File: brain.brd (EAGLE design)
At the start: 100 x 80 mm, 20 parts, among them U1 TINY45-20-DIP, U4 TINY45-20-DIP

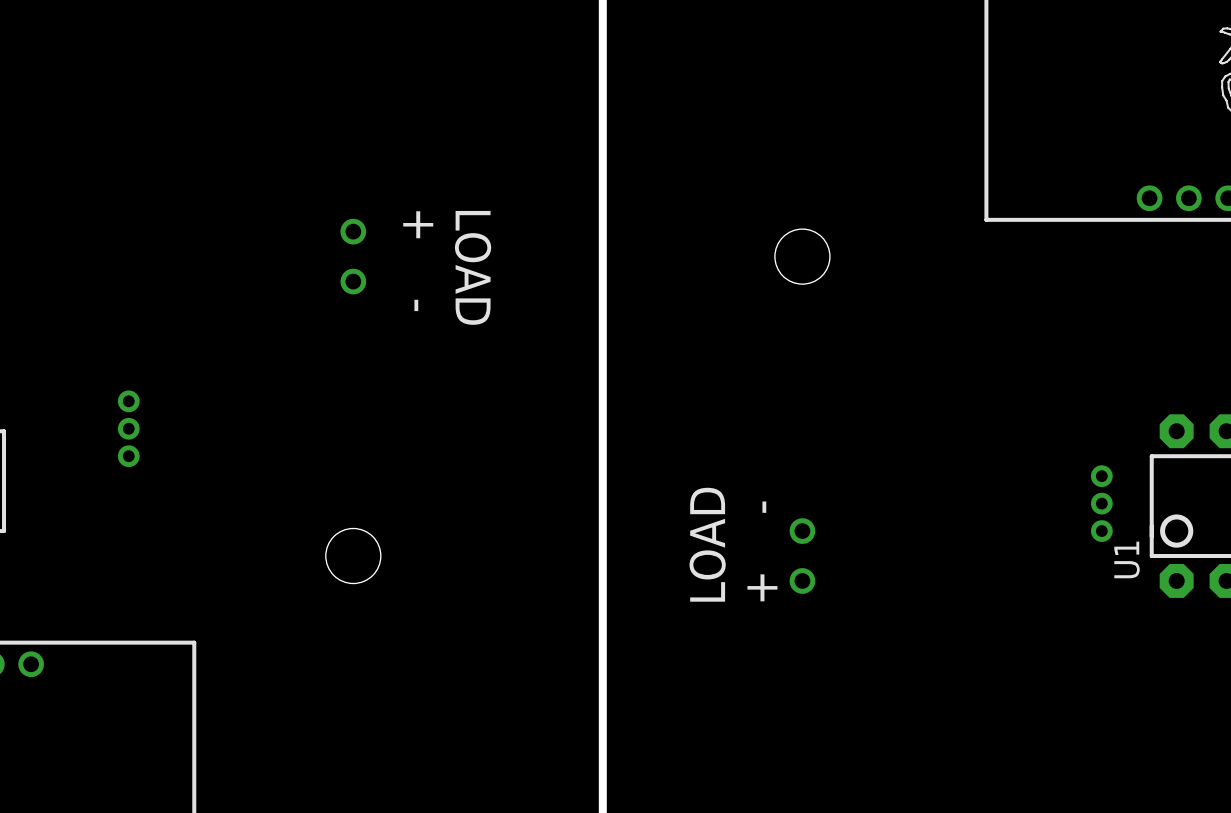
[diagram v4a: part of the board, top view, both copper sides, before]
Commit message: Switched the LDO to the ST device.
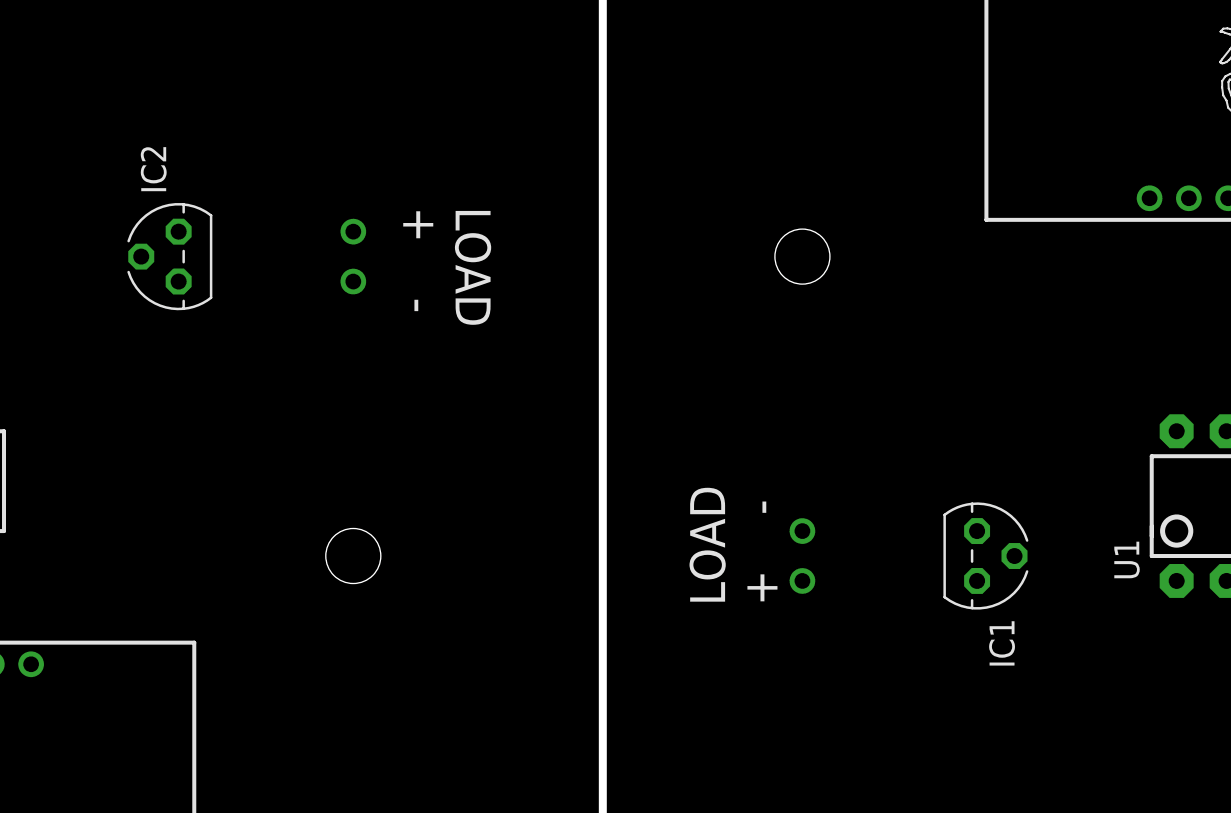
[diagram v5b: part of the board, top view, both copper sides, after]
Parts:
- removed U$2, U$5: LP2950, seniordesign:LP2950
- added IC1, IC2: LP2950ACZ-3.3, v-reg:TO92
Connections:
- net GND1: now also IC1.2; no longer U$2.GND
- net GND2: now also IC2.2; no longer U$5.GND
- net VCC1: now also IC1.1; no longer U$2.VOUT
- net VIN1: now also IC1.3; no longer U$2.VIN
- net VIN2: now also IC2.3; no longer U$5.VIN
- net VOUT2: now also IC2.1; no longer U$5.VOUT
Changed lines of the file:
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@@
 <setting verticaltext="up"/>
 </settings>
-<grid distance="0.05" unitdist="inch" unit="inch" style="dots" multiple="1" display="yes" altdistance="0.025" altunitdist="inch" altunit="inch"/>
+<grid distance="0.05" unitdist="inch" unit="inch" style="dots" multiple="1" display="no" altdistance="0.025" altunitdist="inch" altunit="inch"/>
 <layers>
 <layer number="1" name="Top" color="4" fill="1" visible="yes" active="yes"/>
@@
 <layer number="27" name="tValues" color="7" fill="1" visible="yes" active="yes"/>
 <layer number="28" name="bValues" color="7" fill="1" visible="yes" active="yes"/>
-<layer number="29" name="tStop" color="7" fill="3" visible="no" active="yes"/>
-<layer number="30" name="bStop" color="7" fill="6" visible="no" active="yes"/>
-<layer number="31" name="tCream" color="7" fill="4" visible="no" active="yes"/>
-<layer number="32" name="bCream" color="7" fill="5" visible="no" active="yes"/>
-<layer number="33" name="tFinish" color="6" fill="3" visible="no" active="yes"/>
-<layer number="34" name="bFinish" color="6" fill="6" visible="no" active="yes"/>
-<layer number="35" name="tGlue" color="7" fill="4" visible="no" active="yes"/>
-<layer number="36" name="bGlue" color="7" fill="5" visible="no" active="yes"/>
-<layer number="37" name="tTest" color="7" fill="1" visible="no" active="yes"/>
-<layer number="38" name="bTest" color="7" fill="1" visible="no" active="yes"/>
+<layer number="29" name="tStop" color="7" fill="3" visible="yes" active="yes"/>
+<layer number="30" name="bStop" color="7" fill="6" visible="yes" active="yes"/>
+<layer number="31" name="tCream" color="7" fill="4" visible="yes" active="yes"/>
+<layer number="32" name="bCream" color="7" fill="5" visible="yes" active="yes"/>
+<layer number="33" name="tFinish" color="6" fill="3" visible="yes" active="yes"/>
+<layer number="34" name="bFinish" color="6" fill="6" visible="yes" active="yes"/>
+<layer number="35" name="tGlue" color="7" fill="4" visible="yes" active="yes"/>
+<layer number="36" name="bGlue" color="7" fill="5" visible="yes" active="yes"/>
+<layer number="37" name="tTest" color="7" fill="1" visible="yes" active="yes"/>
+<layer number="38" name="bTest" color="7" fill="1" visible="yes" active="yes"/>
 <layer number="39" name="tKeepout" color="4" fill="11" visible="yes" active="yes"/>
 <layer number="40" name="bKeepout" color="1" fill="11" visible="yes" active="yes"/>
@@
 <layer number="42" name="bRestrict" color="1" fill="10" visible="yes" active="yes"/>
 <layer number="43" name="vRestrict" color="2" fill="10" visible="yes" active="yes"/>
-<layer number="44" name="Drills" color="7" fill="1" visible="no" active="yes"/>
+<layer number="44" name="Drills" color="7" fill="1" visible="yes" active="yes"/>
 <layer number="45" name="Holes" color="7" fill="1" visible="yes" active="yes"/>
-<layer number="46" name="Milling" color="3" fill="1" visible="no" active="yes"/>
-<layer number="47" name="Measures" color="7" fill="1" visible="no" active="yes"/>
+<layer number="46" name="Milling" color="3" fill="1" visible="yes" active="yes"/>
+<layer number="47" name="Measures" color="7" fill="1" visible="yes" active="yes"/>
 <layer number="48" name="Document" color="7" fill="1" visible="yes" active="yes"/>
 <layer number="49" name="Reference" color="7" fill="1" visible="yes" active="yes"/>
@@
 <layer number="100" name="Muster" color="7" fill="1" visible="no" active="no"/>
 <layer number="101" name="Patch_Top" color="12" fill="4" visible="yes" active="yes"/>
-<layer number="102" name="Vscore" color="7" fill="1" visible="yes" active="yes"/>
+<layer number="102" name="Vscore" color="12" fill="1" visible="yes" active="yes"/>
 <layer number="103" name="tMap" color="7" fill="1" visible="yes" active="yes"/>
 <layer number="104" name="Name" color="16" fill="1" visible="yes" active="yes"/>
@@
 <text x="40.64" y="52.07" size="1.778" layer="21" rot="SR270">LOAD
 +    -</text>
+<wire x1="50.8" y1="0" x2="50.8" y2="80.01" width="0.4064" layer="102"/>
 </plain>
 <attributes>
@@
 <element name="U2" library="SparkFun-Connectors" package="AUDIO-JACK" value="" x="95.25" y="22.86" rot="R180"/>
 <element name="U3" library="SparkFun-Connectors" package="AUDIO-JACK" value="" x="95.25" y="8.89" rot="R180"/>
-<element name="U$2" library="seniordesign" package="LP2950" value="LP2950" x="76.2" y="35.56" rot="R90"/>
 <element name="U$3" library="seniordesign" package="SUNNYBUDDYMOUNT" value="SUNNYBUDDYMOUNT" x="59.69" y="49.53"/>
 <element name="XB2" library="maxstream" package="XBEE-PRO" value="XBEE-PRO" x="12.7" y="17.78" rot="R90">
@@
 <attribute name="OC_FARNELL" value="176432" x="-21.59" y="-36.83" size="1.778" layer="27" rot="R90" display="off"/>
 </element>
-<element name="U$5" library="seniordesign" package="LP2950" value="LP2950" x="26.67" y="39.37" rot="R90"/>
 <element name="U$6" library="seniordesign" package="SUNNYBUDDYMOUNT" value="SUNNYBUDDYMOUNT" x="39.37" y="34.29" rot="R180"/>
 <element name="C1" library="rcl" package="C050-025X075" value="bypass" x="12.7" y="2.54"/>
@@
 <attribute name="MF" value="" x="17.78" y="73.66" size="1.778" layer="27" rot="R180" display="off"/>
 </element>
+<element name="IC1" library="v-reg" package="TO92" value="LP2950ACZ-3.3" x="69.85" y="34.29" rot="R270"/>
+<element name="IC2" library="v-reg" package="TO92" value="LP2950ACZ-3.3" x="29.21" y="49.53" rot="R90"/>
 </elements>
 <signals>
@@
 </signal>
 <signal name="VIN2">
-<contactref element="U$5" pad="VIN"/>
 <contactref element="U$6" pad="P$1"/>
-<wire x1="26.67" y1="39.37" x2="38.1" y2="50.8" width="0" layer="19" extent="1-1"/>
+<contactref element="IC2" pad="3"/>
+<wire x1="29.21" y1="50.8" x2="38.1" y2="50.8" width="0" layer="19" extent="1-1"/>
 </signal>
 <signal name="N$8">
@@
 <signal name="VOUT2">
 <contactref element="XB2" pad="1"/>
-<contactref element="U$5" pad="VOUT"/>
 <contactref element="C1" pad="1"/>
 <contactref element="U4" pad="8"/>
 <contactref element="C2" pad="1"/>
-<wire x1="11.43" y1="41.91" x2="26.67" y2="42.164" width="0" layer="19" extent="1-1"/>
+<contactref element="IC2" pad="1"/>
+<wire x1="11.43" y1="41.91" x2="29.21" y2="48.26" width="0" layer="19" extent="1-1"/>
 <wire x1="5.08" y1="40.64" x2="11.43" y2="41.91" width="0" layer="19" extent="1-1"/>
 <wire x1="3.7" y1="6.78" x2="5.08" y2="40.64" width="0" layer="19" extent="1-1"/>
@@
 <contactref element="XB2" pad="10"/>
 <contactref element="S2" pad="2"/>
-<contactref element="U$5" pad="GND"/>
 <contactref element="U$6" pad="P$2"/>
 <contactref element="C1" pad="2"/>
@@
 <contactref element="C2" pad="2"/>
 <contactref element="R3" pad="1"/>
-<wire x1="38.1" y1="48.26" x2="22.86" y2="73.66" width="0" layer="19" extent="1-1"/>
-<wire x1="26.67" y1="40.767" x2="38.1" y2="48.26" width="0" layer="19" extent="1-1"/>
-<wire x1="19.05" y1="34.29" x2="26.67" y2="40.767" width="0" layer="19" extent="1-1"/>
+<contactref element="IC2" pad="2"/>
+<wire x1="27.305" y1="49.53" x2="22.86" y2="73.66" width="0" layer="19" extent="1-1"/>
+<wire x1="38.1" y1="48.26" x2="27.305" y2="49.53" width="0" layer="19" extent="1-1"/>
+<wire x1="19.05" y1="34.29" x2="27.305" y2="49.53" width="0" layer="19" extent="1-1"/>
 <wire x1="5.08" y1="35.56" x2="19.05" y2="34.29" width="0" layer="19" extent="1-1"/>
 <wire x1="21.7" y1="6.78" x2="19.05" y2="34.29" width="0" layer="19" extent="1-1"/>
@@
 <contactref element="XB1" pad="10"/>
 <contactref element="S1" pad="2"/>
-<contactref element="U$2" pad="GND"/>
 <contactref element="U$3" pad="P$2"/>
 <contactref element="C4" pad="2"/>
@@
 <contactref element="R2" pad="2"/>
 <contactref element="C3" pad="2"/>
+<contactref element="IC1" pad="2"/>
 <wire x1="78.63" y1="74.5" x2="85.09" y2="77.47" width="0" layer="19" extent="1-1"/>
 <wire x1="56.1594" y1="74.3712" x2="78.63" y2="74.5" width="0" layer="19" extent="1-1"/>
-<wire x1="76.2" y1="36.957" x2="78.63" y2="74.5" width="0" layer="19" extent="1-1"/>
-<wire x1="87.63" y1="33.02" x2="76.2" y2="36.957" width="0" layer="19" extent="1-1"/>
+<wire x1="60.96" y1="35.56" x2="56.1594" y2="74.3712" width="0" layer="19" extent="1-1"/>
+<wire x1="71.755" y1="34.29" x2="60.96" y2="35.56" width="0" layer="19" extent="1-1"/>
+<wire x1="87.63" y1="33.02" x2="71.755" y2="34.29" width="0" layer="19" extent="1-1"/>
 <wire x1="96.52" y1="34.29" x2="87.63" y2="33.02" width="0" layer="19" extent="1-1"/>
-<wire x1="60.96" y1="35.56" x2="76.2" y2="36.957" width="0" layer="19" extent="1-1"/>
-<wire x1="74.93" y1="17.78" x2="76.2" y2="36.957" width="0" layer="19" extent="1-1"/>
+<wire x1="74.93" y1="17.78" x2="71.755" y2="34.29" width="0" layer="19" extent="1-1"/>
 <wire x1="74.93" y1="3.81" x2="74.93" y2="17.78" width="0" layer="19" extent="1-1"/>
 </signal>
 <signal name="VCC1">
 <contactref element="XB1" pad="1"/>
-<contactref element="U$2" pad="VOUT"/>
 <contactref element="C4" pad="1"/>
 <contactref element="U1" pad="8"/>
 <contactref element="C3" pad="1"/>
+<contactref element="IC1" pad="1"/>
 <wire x1="90.17" y1="77.47" x2="96.63" y2="74.5" width="0" layer="19" extent="1-1"/>
 <wire x1="96.52" y1="39.37" x2="96.63" y2="74.5" width="0" layer="19" extent="1-1"/>
 <wire x1="80.01" y1="40.64" x2="96.52" y2="39.37" width="0" layer="19" extent="1-1"/>
-<wire x1="76.2" y1="38.354" x2="80.01" y2="40.64" width="0" layer="19" extent="1-1"/>
+<wire x1="69.85" y1="35.56" x2="80.01" y2="40.64" width="0" layer="19" extent="1-1"/>
 </signal>
 <signal name="VIN1">
-<contactref element="U$2" pad="VIN"/>
 <contactref element="U$3" pad="P$1"/>
-<wire x1="60.96" y1="33.02" x2="76.2" y2="35.56" width="0" layer="19" extent="1-1"/>
+<contactref element="IC1" pad="3"/>
+<wire x1="69.85" y1="33.02" x2="60.96" y2="33.02" width="0" layer="19" extent="1-1"/>
 </signal>
 <signal name="TX1">

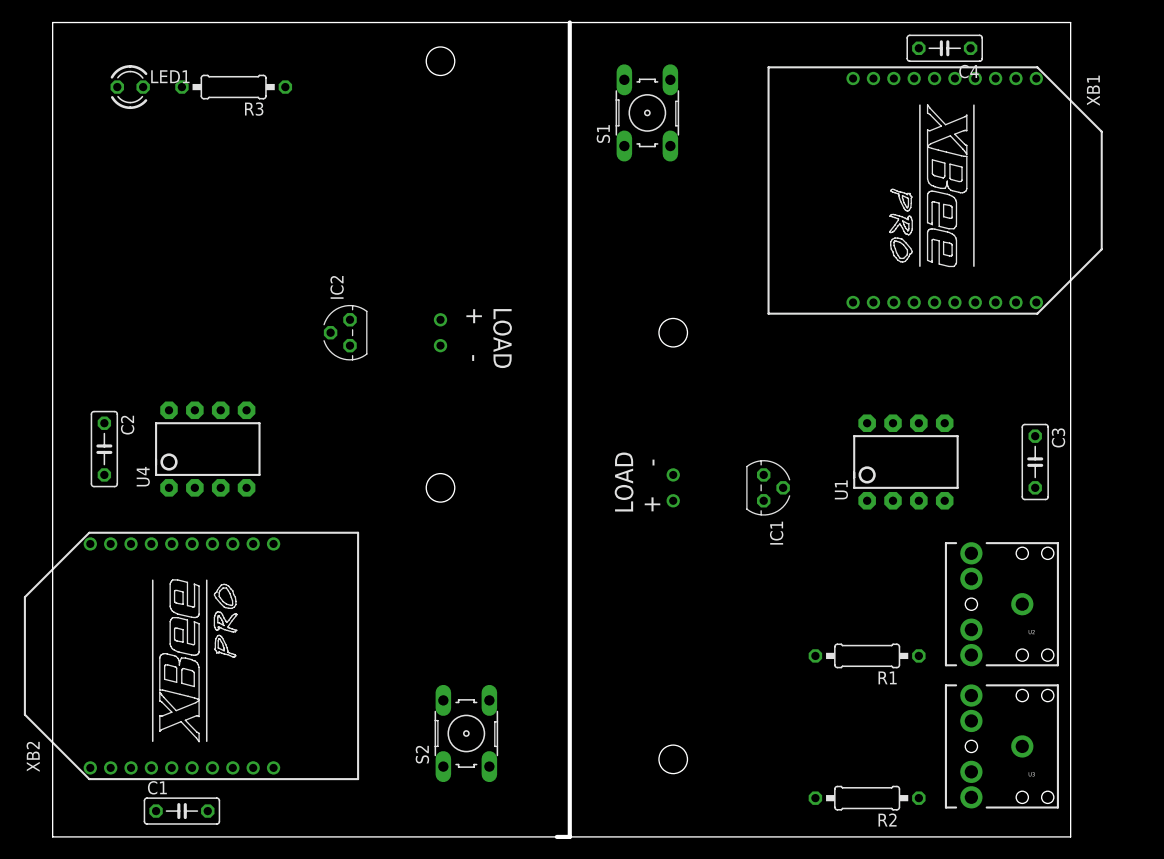
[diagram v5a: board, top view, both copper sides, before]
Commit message: Added test terminals to board. Pre-routing.
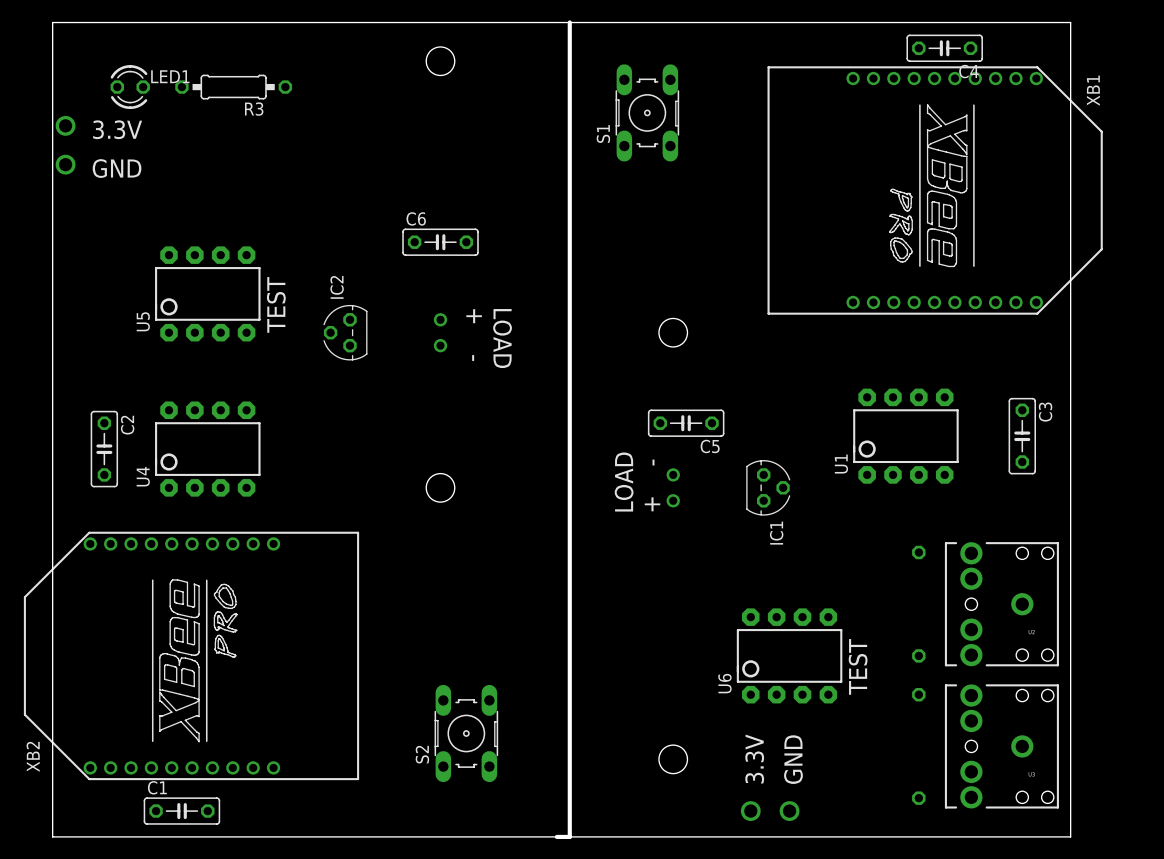
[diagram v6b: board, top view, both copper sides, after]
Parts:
- added C5, C6: bypass, rcl:C050-025X075
- added U5, U6: TINY45-20-DIP, SparkFun-DigitalIC:DIP08
- moved R2 7.18 mm to (85.1, 8.89), flipped to the bottom, turned to 270 degrees
- moved R1 7.18 mm to (85.1, 22.9), flipped to the bottom, turned to 270 degrees
- moved C3 2.84 mm to (95.2, 39.4)
- moved U1 2.54 mm to (83.8, 39.4)
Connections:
- removed net N$1: LED1.A, U4.6
- removed net N$2: R1.1, U1.7, U2.RING
- removed net N$3: R2.1, U1.6, U3.RING
- removed net N$4: U1.5, U2.SLEEVE, U3.SLEEVE
- new net N$14: U5.2
- new net N$7: U4.7
- new net PB01: U1.5, U2.SLEEVE, U3.SLEEVE, U6.5
- new net PB02: U4.5, U5.5
- new net PB11: R2.1, U1.6, U3.RING, U6.6
- new net PB12: LED1.A, U4.6, U5.6
- new net PB21: R1.1, U1.7, U2.RING, U6.7
- new net PB51: U1.1, U6.1
- new net PB52: U4.1, U5.1
- net GND1: now also C5.2, U6.4
- net GND2: now also C6.2, U5.4
- net RX1: now also U6.3
- net RX2: now also U5.3
- net TX1: now also U6.2
- net TX2: now also U5.7
- net VCC1: now also U6.8
- net VIN1: now also C5.1
- net VIN2: now also C6.1
- net VOUT2: now also U5.8
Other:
- board text added: "3.3V"
- board text added: "GND"
- board text added: "TEST"
